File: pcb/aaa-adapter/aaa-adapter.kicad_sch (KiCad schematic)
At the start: 2 parts

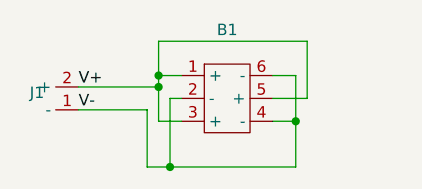
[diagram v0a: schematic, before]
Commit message: Remove the need for a 3d print?
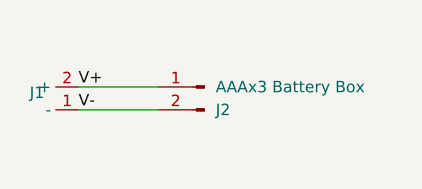
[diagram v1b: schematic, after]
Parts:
- removed B1: ~, aaa:aaa-holder-3x1-pins, symbol aaa:aaa-holder
- added J2: AAAx3 Battery Box, Battery:BatteryHolder_Keystone_2479_3xAAA, symbol Connector:Conn_01x02_Pin
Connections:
- net V+: now also J2.1 (Pin_1)
- net V-: now also J2.2 (Pin_2)
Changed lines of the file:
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@@
 	(generator_version "8.0")
 	(paper "A4")
-	(junction
-		(at 86.36 31.75)
-		(diameter 0)
-		(color 0 0 0 0)
-	)
-	(junction
-		(at 71.12 27.94)
-		(diameter 0)
-		(color 0 0 0 0)
-	)
-	(junction
-		(at 72.39 36.83)
-		(diameter 0)
-		(color 0 0 0 0)
-	)
-	(junction
-		(at 71.12 26.67)
-		(diameter 0)
-		(color 0 0 0 0)
-	)
-	(wire
-		(pts
-			(xy 86.36 31.75) (xy 86.36 36.83)
-		)
-		(stroke
-			(width 0)
-			(type default)
-		)
-	)
-	(wire
-		(pts
-			(xy 87.63 22.86) (xy 71.12 22.86)
-		)
-		(stroke
-			(width 0)
-			(type default)
-		)
-	)
-	(wire
-		(pts
-			(xy 86.36 26.67) (xy 86.36 31.75)
-		)
-		(stroke
-			(width 0)
-			(type default)
-		)
-	)
-	(wire
-		(pts
-			(xy 72.39 29.21) (xy 72.39 36.83)
-		)
-		(stroke
-			(width 0)
-			(type default)
-		)
-	)
-	(wire
-		(pts
-			(xy 72.39 36.83) (xy 69.85 36.83)
-		)
-		(stroke
-			(width 0)
-			(type default)
-		)
-	)
-	(wire
-		(pts
-			(xy 72.39 36.83) (xy 86.36 36.83)
-		)
-		(stroke
-			(width 0)
-			(type default)
-		)
-	)
-	(wire
-		(pts
-			(xy 87.63 29.21) (xy 87.63 22.86)
-		)
-		(stroke
-			(width 0)
-			(type default)
-		)
-	)
-	(wire
-		(pts
-			(xy 83.82 29.21) (xy 87.63 29.21)
-		)
-		(stroke
-			(width 0)
-			(type default)
-		)
-	)
-	(wire
-		(pts
-			(xy 71.12 27.94) (xy 71.12 26.67)
-		)
-		(stroke
-			(width 0)
-			(type default)
-		)
-	)
-	(wire
-		(pts
-			(xy 83.82 31.75) (xy 86.36 31.75)
-		)
-		(stroke
-			(width 0)
-			(type default)
-		)
-	)
 	(wire
 		(pts
@@
 	(wire
 		(pts
-			(xy 62.23 30.48) (xy 69.85 30.48)
-		)
-		(stroke
-			(width 0)
-			(type default)
-		)
-	)
-	(wire
-		(pts
-			(xy 73.66 31.75) (xy 71.12 31.75)
-		)
-		(stroke
-			(width 0)
-			(type default)
-		)
-	)
-	(wire
-		(pts
-			(xy 69.85 30.48) (xy 69.85 36.83)
-		)
-		(stroke
-			(width 0)
-			(type default)
-		)
-	)
-	(wire
-		(pts
-			(xy 83.82 26.67) (xy 86.36 26.67)
-		)
-		(stroke
-			(width 0)
-			(type default)
-		)
-	)
-	(wire
-		(pts
-			(xy 72.39 29.21) (xy 73.66 29.21)
-		)
-		(stroke
-			(width 0)
-			(type default)
-		)
-	)
-	(wire
-		(pts
-			(xy 71.12 22.86) (xy 71.12 26.67)
-		)
-		(stroke
-			(width 0)
-			(type default)
-		)
-	)
-	(wire
-		(pts
-			(xy 73.66 26.67) (xy 71.12 26.67)
-		)
-		(stroke
-			(width 0)
-			(type default)
-		)
-	)
-	(wire
-		(pts
-			(xy 71.12 31.75) (xy 71.12 27.94)
+			(xy 62.23 30.48) (xy 71.12 30.48)
 		)
 		(stroke
@@
 	)
 	(symbol
-		(lib_id "aaa:aaa-holder")
-		(at 73.66 26.67 0)
+		(lib_id "Connector:Conn_01x02_Pin")
+		(at 76.2 27.94 0)
+		(mirror y)
 		(unit 1)
 		(exclude_from_sim no)
@@
 		(on_board yes)
 		(dnp no)
-		(fields_autoplaced yes)
-		(property "Reference" "B1"
-			(at 78.74 21.59 0)
+		(property "Reference" "J2"
+			(at 77.47 30.4801 0)
 			(effects
 				(font
 					(size 1.27 1.27)
 				)
+				(justify right)
 			)
 		)
-		(property "Value" "~"
-			(at 78.74 24.13 0)
+		(property "Value" "AAAx3 Battery Box"
+			(at 77.47 27.9401 0)
 			(effects
 				(font
 					(size 1.27 1.27)
 				)
+				(justify right)
 			)
 		)
-		(property "Footprint" "aaa:aaa-holder-3x1-pins"
-			(at 73.66 26.67 0)
+		(property "Footprint" "Battery:BatteryHolder_Keystone_2479_3xAAA"
+			(at 76.2 27.94 0)
 			(effects
 				(font
@@
 			)
 		)
-		(property "Datasheet" ""
-			(at 73.66 26.67 0)
+		(property "Datasheet" "~"
+			(at 76.2 27.94 0)
 			(effects
 				(font
@@
 			)
 		)
-		(property "Description" ""
-			(at 73.66 26.67 0)
+		(property "Description" "Generic connector, single row, 01x02, script generated"
+			(at 76.2 27.94 0)
 			(effects
 				(font
@@
 		(pin "2"
 		)
-		(pin "6"
-		)
-		(pin "3"
-		)
-		(pin "5"
-		)
 		(pin "1"
-		)
-		(pin "4"
 		)
 		(instances
 			(project ""
 				(path "/41aac83e-6a36-47a6-b594-964fc9079efb"
-					(reference "B1")
+					(reference "J2")
 					(unit 1)
 				)
